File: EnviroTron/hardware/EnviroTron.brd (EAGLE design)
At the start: 27.3 x 36.8 mm, 31 parts

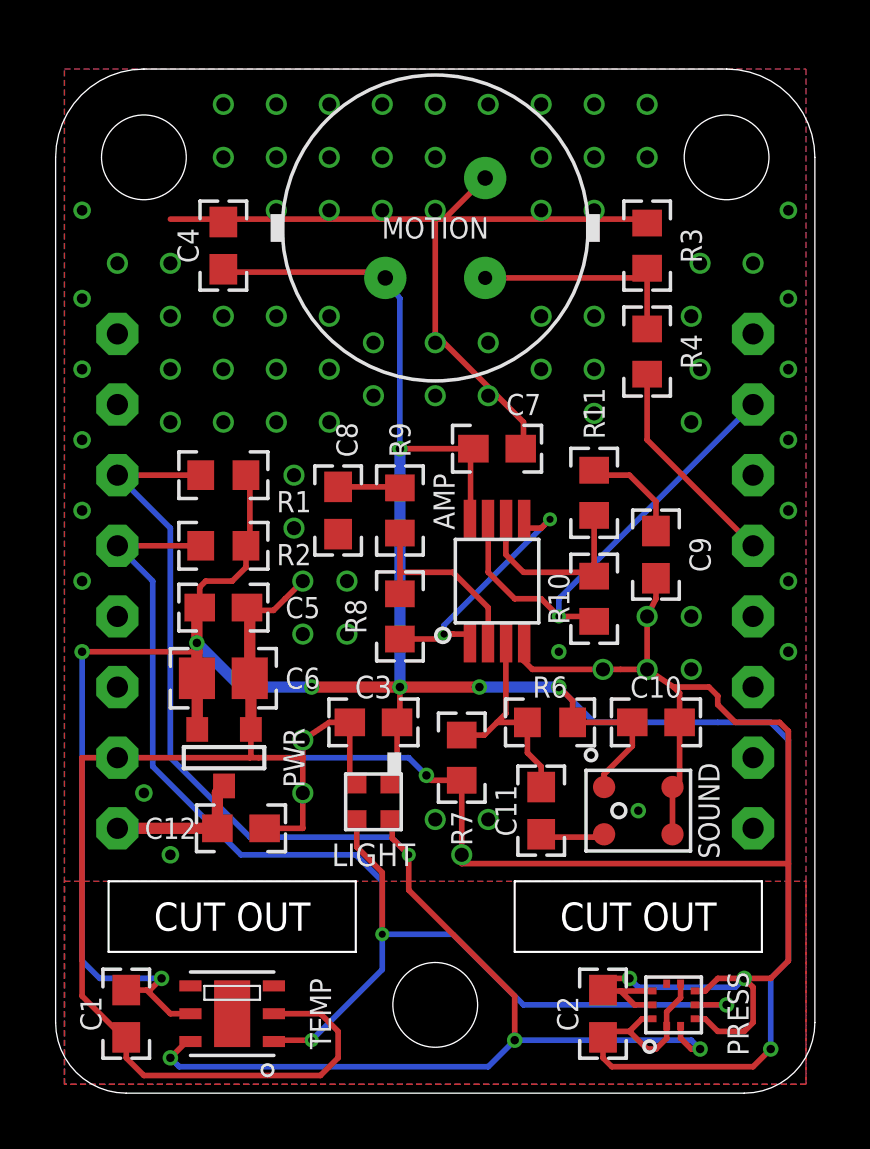
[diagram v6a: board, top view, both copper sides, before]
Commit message: Added ADC in place of noisy ESP8266 ADC. Switched to precision reference for voltage source.
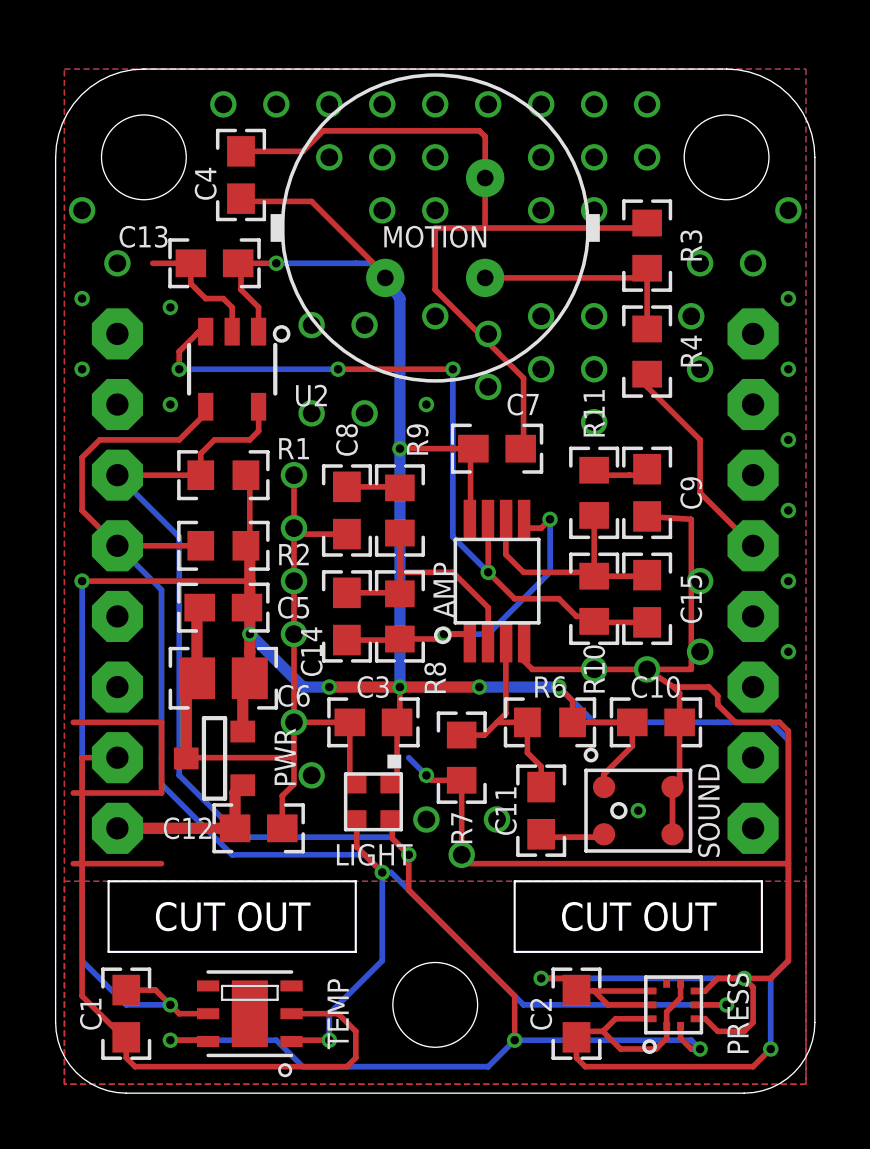
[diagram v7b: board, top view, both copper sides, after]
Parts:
- added C13: 100n, EnviroTron:C0603
- added C14, C15: 1n, EnviroTron:C0603
- added U2: MCP3221, EnviroTron:SOT23-5
- PWR: value MCP1700-SOT23 -> VREG-REF33XX-SOT23
- moved C4 2.62 mm to (6.67, 33.0)
- moved C9 2.25 mm to (21.3, 21.6)
- moved C2 0.95 mm to (18.7, 2.86)
- moved TEMP 0.64 mm to (6.99, 2.86)
- moved C12 0.63 mm to (7.30, 9.53)
- moved PWR 0.32 mm to (5.71, 12.1), turned to 0 degrees
- moved C8 0.32 mm to (10.5, 21.0)
- turned C5 to 180 degrees
- turned C6 to 180 degrees
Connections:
- net +5V: now also PWR.1; no longer PWR.3
- net 3V3: now also C13.1, U2.1
- net AMP_OUT: now also C15.1, U2.3; no longer COMMS.A0
- net GND: now also C13.2, PWR.3, U2.2; no longer PWR.1
- net N$2: now also C14.1
- net N$6: now also C14.2
- net N$9: now also C15.2
- net SCL: now also U2.5
- net SDA: now also U2.4
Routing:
- net GND: track 143.3 -> 172.7 mm, vias 89 -> 67
- net 3V3: track 116.5 -> 130.8 mm, vias 9 -> 10
- net AMP_OUT: track 17.5 -> 28.5 mm, vias 1 -> 4
- net SDA: track 48.6 -> 56.5 mm
- net SCL: track 55.7 -> 60.7 mm
- net N$2: track 10.00 -> 12.9 mm
- net N$9: track 6.87 -> 9.41 mm
- net N$6: track 7.13 -> 9.08 mm
- net N$10: track 3.72 -> 2.65 mm
- net +5V: track 5.22 -> 5.90 mm

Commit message: Changed mic to new part. Added Pi filter for analog voltage rail.
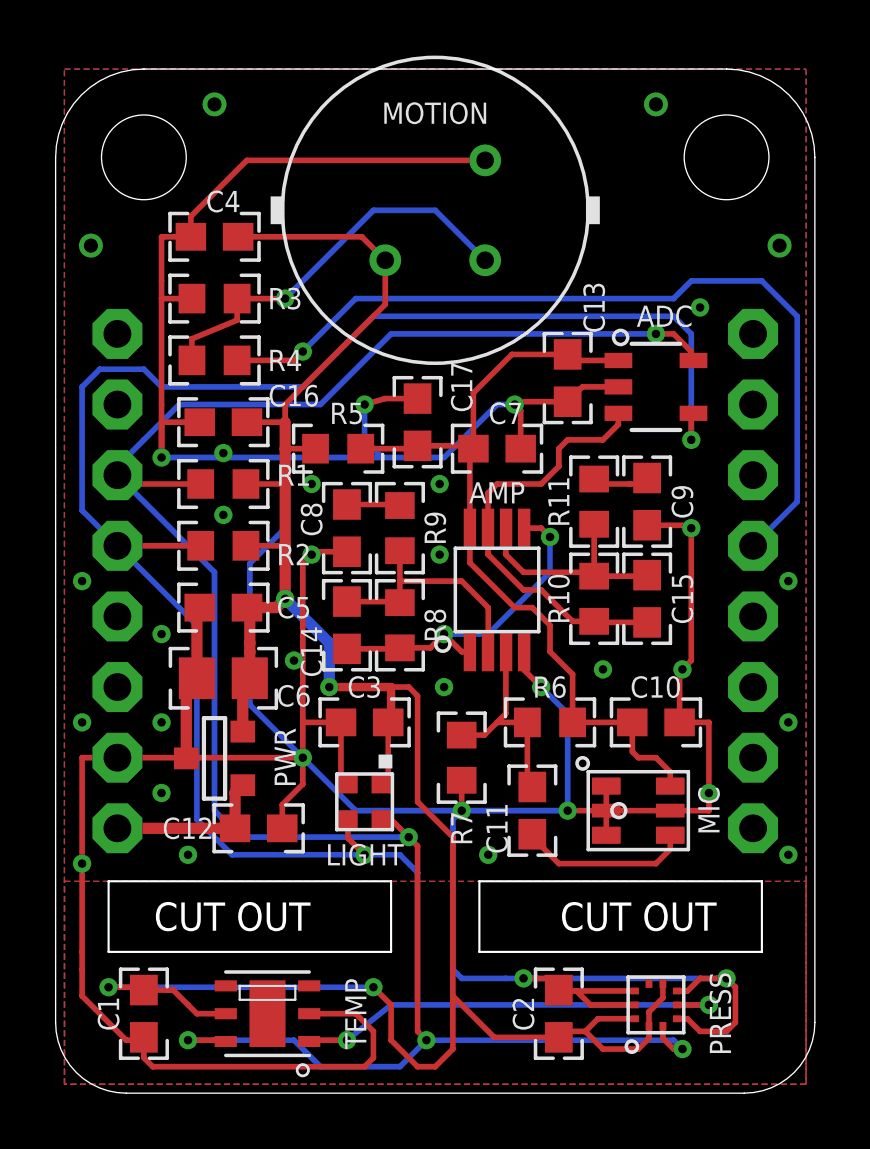
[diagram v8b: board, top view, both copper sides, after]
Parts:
- removed SOUND: SPU0410HR5H, EnviroTron:BPAD-4
- removed U2: MCP3221, EnviroTron:SOT23-5
- added ADC: MCP3221, EnviroTron:SOT23-5
- added C16, C17: 1u, EnviroTron:C0603
- added MIC: MIC-MEMS-6, EnviroTron:DFN-6
- added R5: 100, EnviroTron:R0603
- C14, C15: value 1n -> 100p
- R10, R8: value 68k -> 180k
- moved R3 15.7 mm to (5.71, 28.6), turned to 180 degrees
- moved R4 15.6 mm to (5.71, 26.4), turned to 0 degrees
- moved C13 13.4 mm to (18.4, 25.7), turned to 270 degrees
- moved C4 2.42 mm to (5.71, 30.8), turned to 180 degrees
- moved C2 0.64 mm to (18.1, 2.86)
- moved MOTION 0.64 mm to (13.7, 31.8)
- moved PRESS 0.64 mm to (21.6, 3.17)
- moved C1 0.63 mm to (3.17, 2.86)
- moved TEMP 0.63 mm to (7.62, 2.86)
- moved C8 0.63 mm to (10.5, 20.3)
- moved R9 0.63 mm to (12.4, 20.3)
- moved R1 0.32 mm to (6.03, 21.9)
- moved AMP 0.32 mm to (15.9, 18.1)
- moved C11 0.32 mm to (17.1, 10.2)
- moved C14 0.32 mm to (10.5, 16.8)
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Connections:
- removed net AMP_OUT: AMP.7, C15.1, R10.1, U2.3
- new net 3V3A: ADC.1, AMP.8, C10.1, C13.1, C17.1, C7.1, MIC.6, R5.2, R6.1
- new net MIC_SIG: ADC.3, AMP.7, C15.1, R10.1
- net 3V3: now also C16.1, R5.1; no longer AMP.8, C10.1, C13.1, C7.1, R6.1, SOUND.1, U2.1
- net GND: now also ADC.2, C16.2, C17.2, MIC.1, MIC.2, MIC.3, MIC.5; no longer SOUND.2, SOUND.3, U2.2
- net N$8: now also MIC.4; no longer SOUND.4
- net SCL: now also ADC.5; no longer U2.5
- net SDA: now also ADC.4; no longer U2.4
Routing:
- net 3V3: track 130.8 -> 88.2 mm, vias 10 -> 4
- net 3V3A: track 0.00 -> 29.1 mm
- net AMP_OUT: track 28.5 -> 0.00 mm, vias 4 -> 0
- net SDA: track 56.5 -> 79.8 mm, vias 3 -> 4
- net PIROUT: track 7.75 -> 30.8 mm, vias 0 -> 1
- net SCL: track 60.7 -> 77.7 mm, vias 4 -> 5
- net MIC_SIG: track 0.00 -> 15.4 mm
- net GND: track 172.7 -> 179.6 mm, vias 67 -> 37
- net N$3: track 8.33 -> 14.3 mm, vias 0 -> 1
- net N$8: track 2.44 -> 6.28 mm
- net N$2: track 12.9 -> 12.1 mm
- net N$9: track 9.41 -> 8.84 mm
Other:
- outline, holes or cut-outs redrawn
